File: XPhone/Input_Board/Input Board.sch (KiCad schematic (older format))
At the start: 93 parts, among them J1 AUDIO, J10 ENV, J11 PULSE, J12 PULSE, J13 Power In, J14 Power Out, J2 AUDIO, J3 ENV, J4 ENV, J5 PULSE, J6 PULSE, J7 AUDIO, J8 AUDIO, J9 ENV, Q1 BC847CW, Q2 BC847CW, Q3 BC847CW, Q4 BC847CW, Q5 BC847CW, Q6 BC847CW, Q7 BC847CW, Q8 BC847CW, Q9 BC847CW, U1 LM833, U2 78L05, U3 TL084, U4 74HC14, U5 LM833

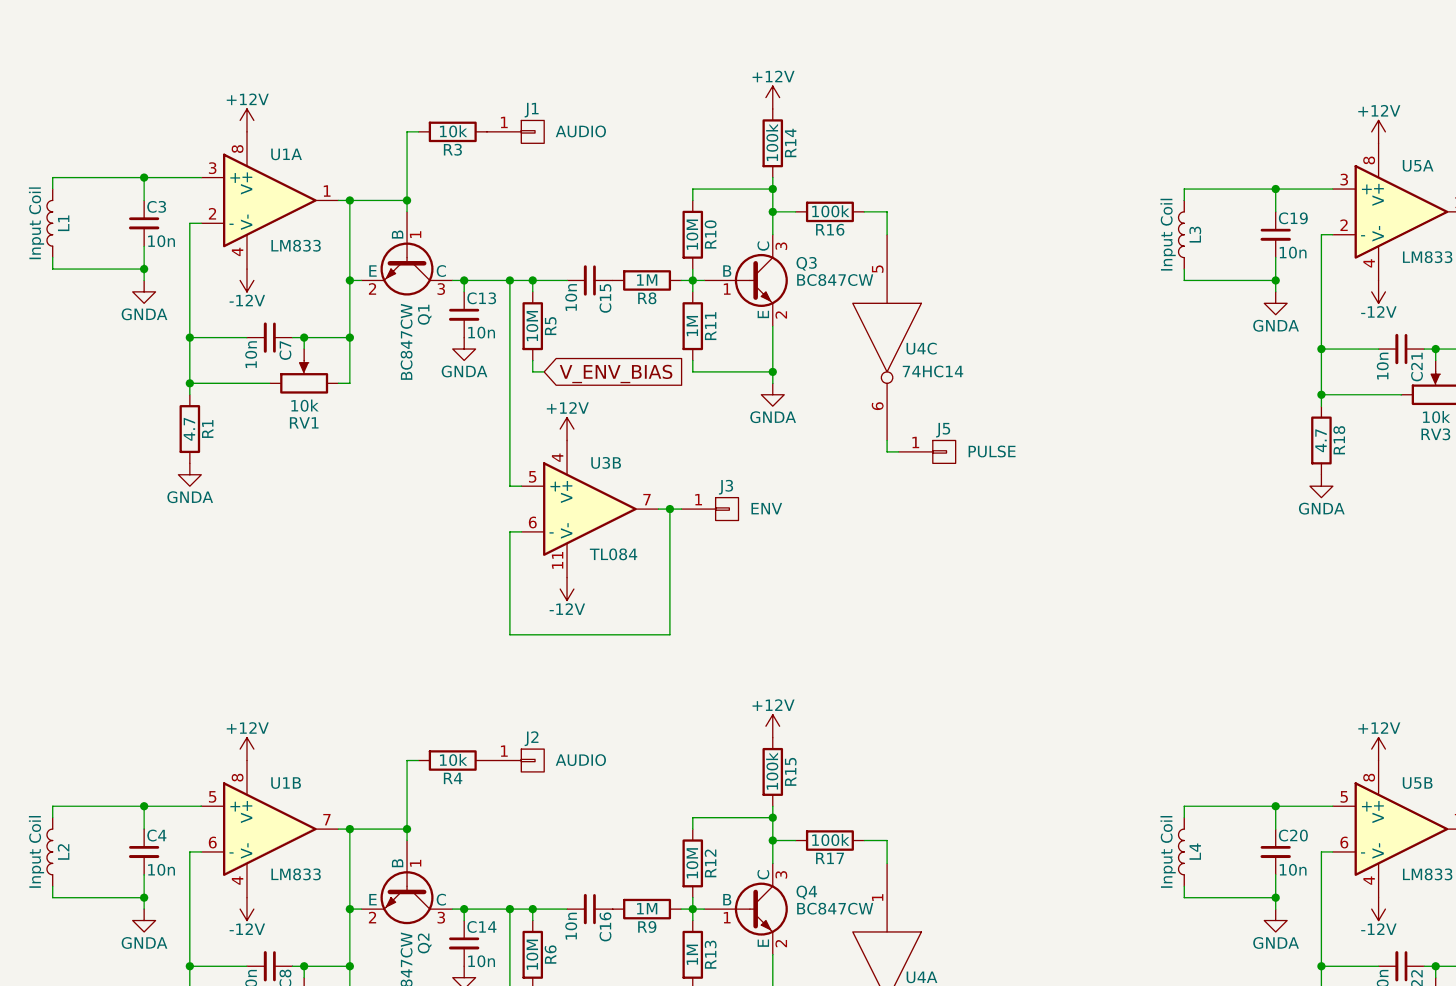
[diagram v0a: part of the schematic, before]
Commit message: polishing the F.Fab layer
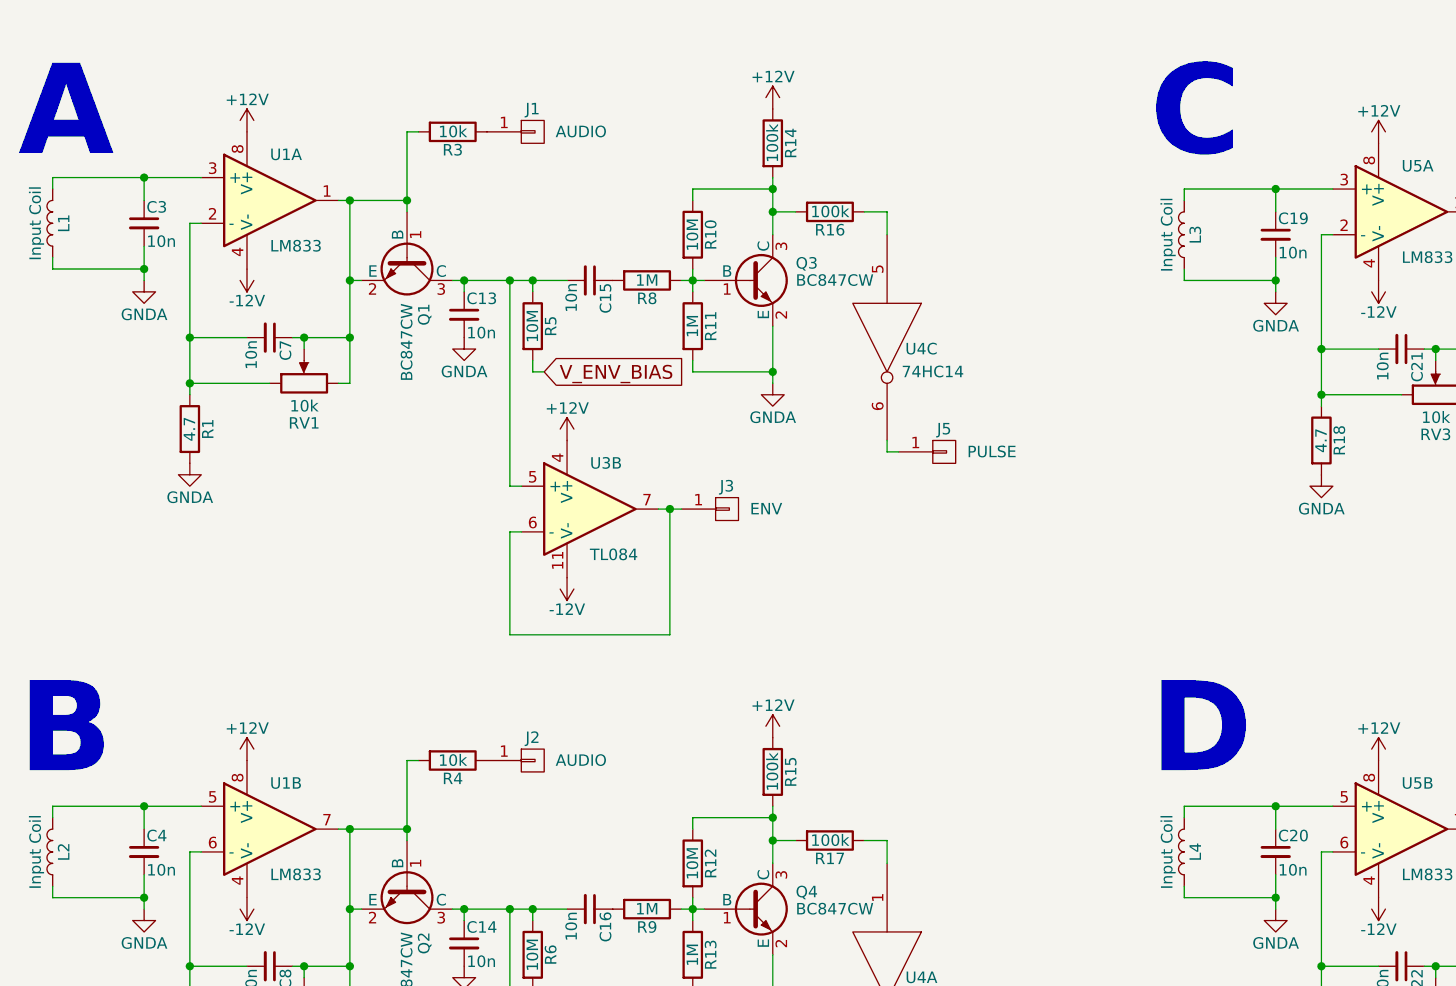
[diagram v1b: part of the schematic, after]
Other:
- note added: "A"
- note added: "B"
- note added: "C"
- note added: "D"
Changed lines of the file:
@@
 Text GLabel 5000 6650 2    60   Input ~ 0
 V_ENV_BIAS
+Text Notes 550  1000 0    394  ~ 79
+A
+Text Notes 550  3700 0    394  ~ 79
+B
+Text Notes 5500 3700 0    394  ~ 79
+D
+Text Notes 5500 1000 0    394  ~ 79
+C
 $EndSCHEMATC
